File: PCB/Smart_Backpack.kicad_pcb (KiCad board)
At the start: 2 copper layers, 65.8 x 74.4 mm, 62 parts, among them J1 Conn_01x03_Pin, J10 Conn_01x02_Pin, J2 Conn_01x02_Pin, J3 Conn_01x02_Pin, J4 Conn_01x03_Pin, J5 Conn_01x03_Pin, J6 Conn_01x03_Pin, J7 Conn_01x07_Pin, J8 Conn_01x08_Socket, J9 USB_C_Receptacle_USB2.0_16P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

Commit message: Start of feedback implementation
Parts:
- removed C14, C15: 0.1uF, Capacitor_SMD:C_1206_3216Metric_Pad1.33x1.80mm_HandSolder
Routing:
- net Net-(U1-SW): track 12.7 -> 2.97 mm
- net +5V: track 51.2 -> 46.3 mm, vias 1 -> 0
- net GND: track 81.0 -> 78.4 mm
- net +3V3: track 250.2 -> 250.9 mm

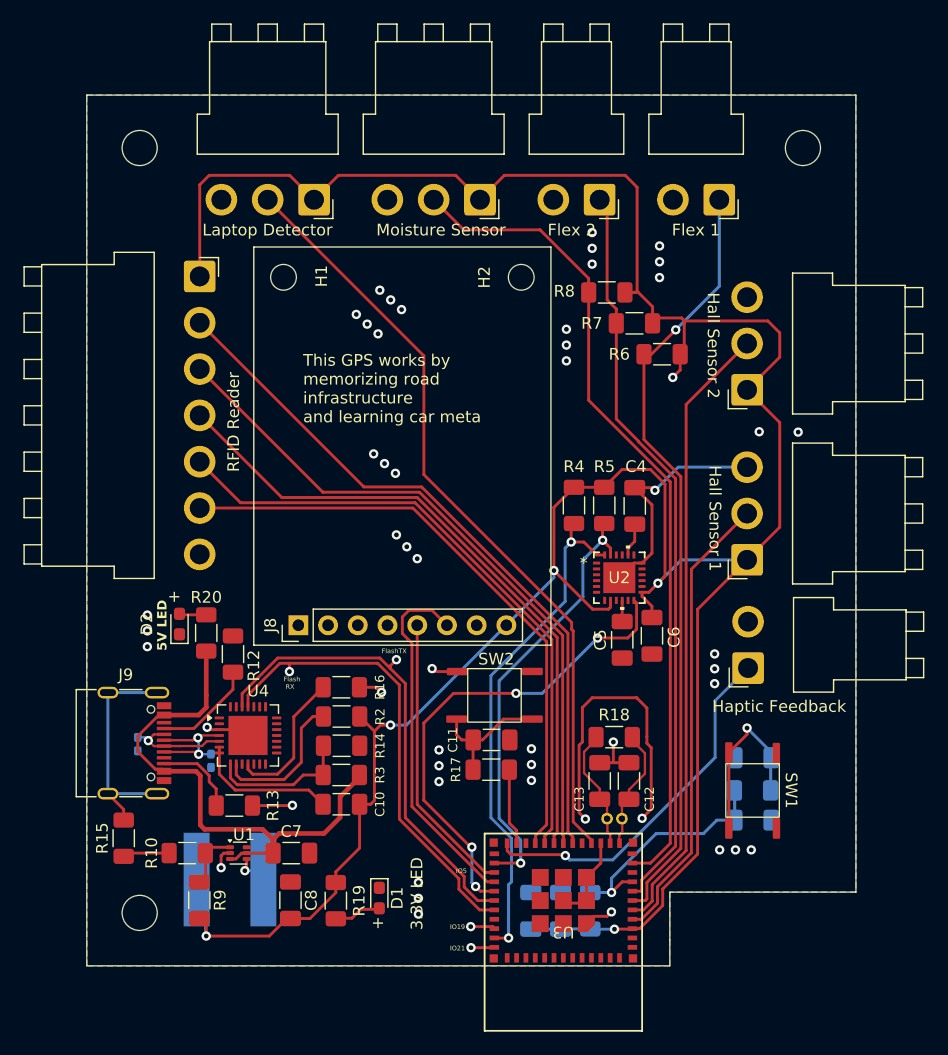
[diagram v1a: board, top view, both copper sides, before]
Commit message: Implemented all feedback except buck converter
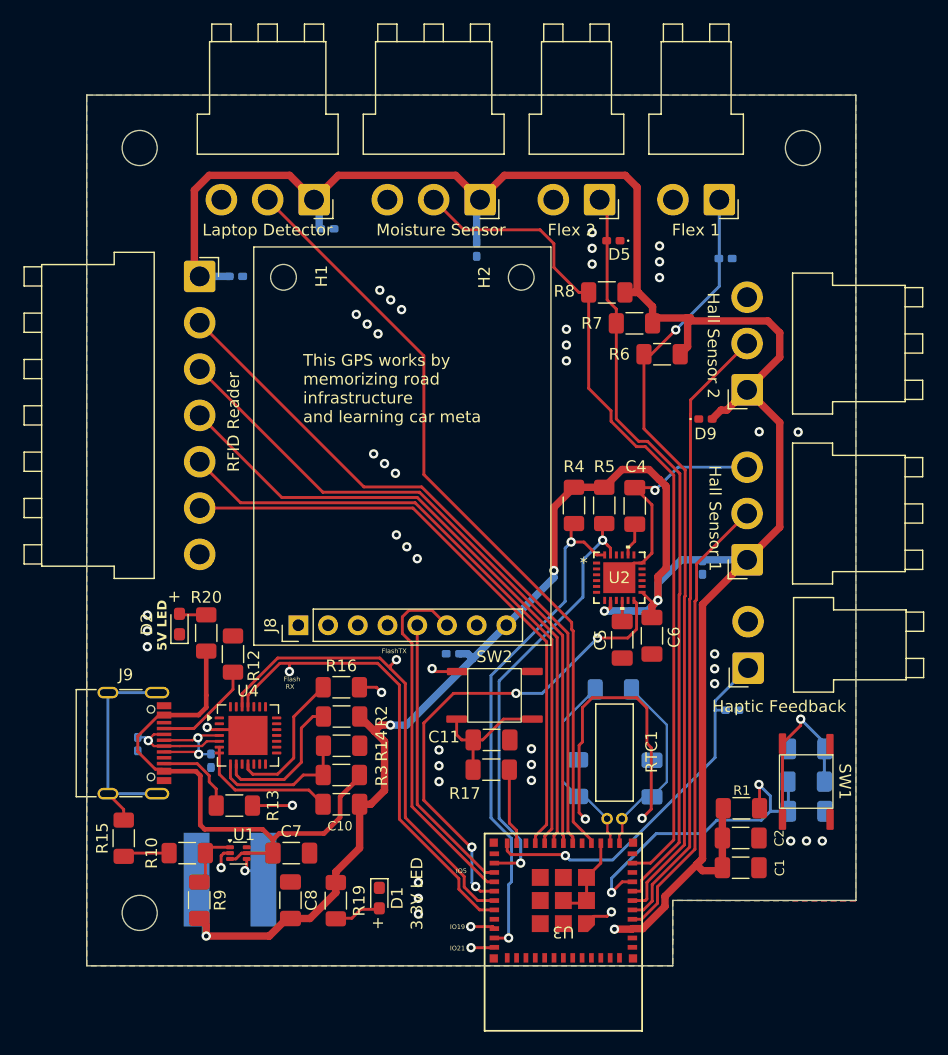
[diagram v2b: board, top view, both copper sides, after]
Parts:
- added D10: ESD321, Diode_SMD:D_0402_1005Metric_Pad0.77x0.64mm_HandSolder, B.Cu at (137.9, 80.0)
- added D11: ESD321, Diode_SMD:D_0402_1005Metric_Pad0.77x0.64mm_HandSolder, B.Cu at (98.0, 55.1)
- added D12: ESD321, Diode_SMD:D_0402_1005Metric_Pad0.77x0.64mm_HandSolder, B.Cu at (105.9, 51.1)
- added D13: ESD321, Diode_SMD:D_0402_1005Metric_Pad0.77x0.64mm_HandSolder, B.Cu at (116.6, 87.4)
- added D5: ESD321, Diode_SMD:D_0402_1005Metric_Pad0.77x0.64mm_HandSolder, F.Cu at (130.3, 52.1)
- added D6: ESD321, Diode_SMD:D_0402_1005Metric_Pad0.77x0.64mm_HandSolder, B.Cu at (139.9, 53.6)
- added D7: ESD321, Diode_SMD:D_0402_1005Metric_Pad0.77x0.64mm_HandSolder, B.Cu at (118.6, 52.8)
- added D8: ESD321, Diode_SMD:D_0402_1005Metric_Pad0.77x0.64mm_HandSolder, B.Cu at (140.5, 92.2)
- added D9: ESD321, Diode_SMD:D_0402_1005Metric_Pad0.77x0.64mm_HandSolder, F.Cu at (138.2, 67.3)
- C1, C2, R1, RTC1: moved to F.Cu
- C12, C13, R18: moved to B.Cu
- R11: value 5Ω -> 0Ω
- R4, R5: value 10kΩ -> 4.7kΩ
- moved C1 18.3 mm to (141.2, 105.7), turned to 0 degrees
- moved C2 16.6 mm to (141.2, 103.1), turned to 0 degrees
- moved R1 15.6 mm to (141.2, 100.6), turned to 0 degrees
- moved C3 4.65 mm to (146.8, 100.8)
- moved C9 4.65 mm to (146.8, 95.5)
- moved R11 4.65 mm to (146.8, 98.3)
- moved SW1 4.65 mm to (146.8, 98.3)
- moved C13 4.47 mm to (133.6, 98.0)
- moved C12 4.39 mm to (127.3, 98.0)
- moved R18 4.08 mm to (130.3, 90.4), turned to 0 degrees
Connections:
- U3 pad 22: unconnected-(U3-IO2-Pad22) -> GND
- U4 pad 23: CTS -> GND
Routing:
- net +3V3: track 250.9 -> 267.5 mm
- net ESP_EN: track 20.4 -> 28.2 mm, vias 1 -> 2
- net RTC_XN: track 10.4 -> 16.5 mm
- net RTC_XP: track 10.4 -> 16.3 mm
- net GND: track 78.4 -> 73.7 mm, vias 51 -> 50
- net MOIST_SIG: track 71.2 -> 72.3 mm
- net MOTOR: track 31.1 -> 32.0 mm
- net FLEX_2: track 63.8 -> 64.5 mm
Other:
- outline, holes or cut-outs redrawn

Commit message: This time for sure...
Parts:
- C7, C8, R10, R9, U1: moved to B.Cu
- moved D1 15.5 mm to (95.0, 106.0), turned to 0 degrees
- moved R9 15.0 mm to (102.5, 95.6), turned to 0 degrees
- moved R19 10.9 mm to (95.8, 109.5), turned to 90 degrees
- moved R10 10.8 mm to (102.5, 98.0)
- moved C8 8.23 mm to (98.8, 101.2)
- moved C7 6.60 mm to (107.8, 100.2), turned to 90 degrees
- moved U1 5.83 mm to (103.3, 101.5), turned to 180 degrees
- moved L1 4.37 mm to (101.6, 108.4)
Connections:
- U3 pad 12: RTC_XP -> RTC_XN
- U3 pad 13: RTC_XN -> RTC_XP
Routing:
- net +3V3: track 267.5 -> 276.0 mm
- net +5V: track 46.3 -> 42.3 mm, vias 0 -> 1
- net Net-(U1-SW): track 2.97 -> 0.00 mm, vias 1 -> 0
- net Net-(D1-A): track 4.16 -> 1.98 mm
- net GND: track 73.7 -> 74.1 mm, vias 50 -> 48
- added copper zone on B.Cu, net +5V
- added copper zone on B.Cu, net Net-(U1-SW)

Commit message: add new feedback
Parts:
- moved C1 2.54 mm to (141.2, 103.1)
- moved C2 2.54 mm to (141.2, 105.7)
- moved R18 0.16 mm to (130.3, 90.3)
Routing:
- net GND: track 74.1 -> 83.7 mm, vias 48 -> 49
- net +3V3: track 276.0 -> 271.0 mm
- net MOTOR: track 32.0 -> 33.9 mm
- net ESP_EN: track 28.2 -> 27.5 mm

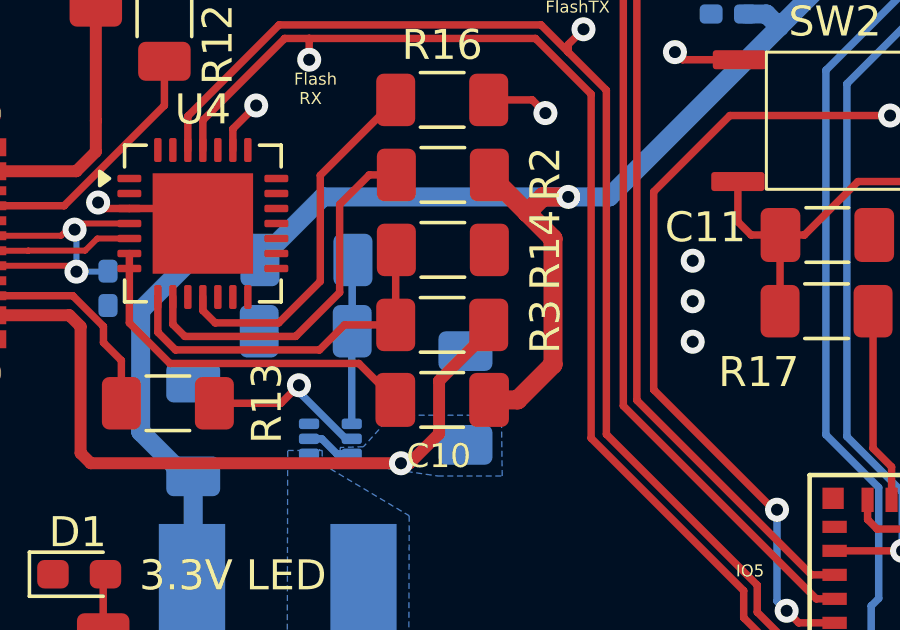
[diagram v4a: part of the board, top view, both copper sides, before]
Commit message: add one singular via
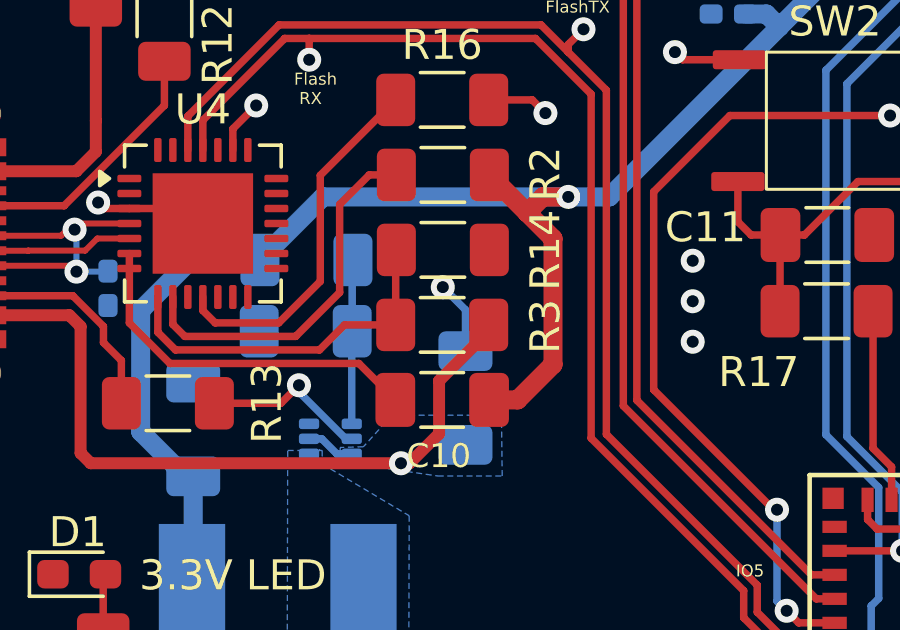
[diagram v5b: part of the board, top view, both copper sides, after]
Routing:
- net GND: track 83.7 -> 86.2 mm, vias 49 -> 50
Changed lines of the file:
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@@
+	)
+	(via
+		(at 107.07 96.48)
+		(size 0.8)
+		(drill 0.4)
+		(layers "F.Cu" "B.Cu")
+		(net 1)
 	)
 	(via
@@
 	)
 	(segment
+		(start 107.825 98.6125)
+		(end 107.825 97.235)
+		(width 0.25)
+		(layer "B.Cu")
+		(net 1)
+	)
+	(segment
 		(start 125.558 90.952)
 		(end 125.558 99.756014)
@@
 		(width 0.25)
 		(layer "B.Cu")
+		(net 1)
+	)
+	(segment
+		(start 107.825 97.235)
+		(end 107.07 96.48)
+		(width 0.25)
+		(layer "B.Cu")

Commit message: fix power layout again
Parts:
- moved R9 9.57 mm to (97.7, 103.8), turned to 90 degrees
- moved L1 9.36 mm to (110.7, 106.2), turned to -90 degrees
- moved C8 9.24 mm to (103.5, 109.2), turned to 180 degrees
- moved R10 6.40 mm to (100.1, 103.9), turned to -90 degrees
- moved C7 5.76 mm to (102.3, 98.5), turned to 180 degrees
- moved U1 1.54 mm to (103.7, 103.0), turned to -90 degrees
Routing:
- net +3V3: track 271.0 -> 277.5 mm, vias 6 -> 10
- net +5V: track 42.3 -> 44.5 mm
- net GND: track 86.2 -> 85.7 mm, vias 50 -> 51
- added copper zone on B.Cu, net +3V3

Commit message: PCB finished and ordered
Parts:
- added R21: 10 kΩ, Resistor_SMD:R_1206_3216Metric_Pad1.30x1.75mm_HandSolder, F.Cu at (119.8, 99.7)
- R17: value 5Ω -> 0Ω
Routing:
- net +3V3: track 277.5 -> 280.8 mm, vias 10 -> 11
